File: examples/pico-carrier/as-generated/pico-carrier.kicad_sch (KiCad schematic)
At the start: 9 parts, among them J1 5V IN, J3 GP0-GP15, J4 GP16-GP28, PWR, U1 Pico

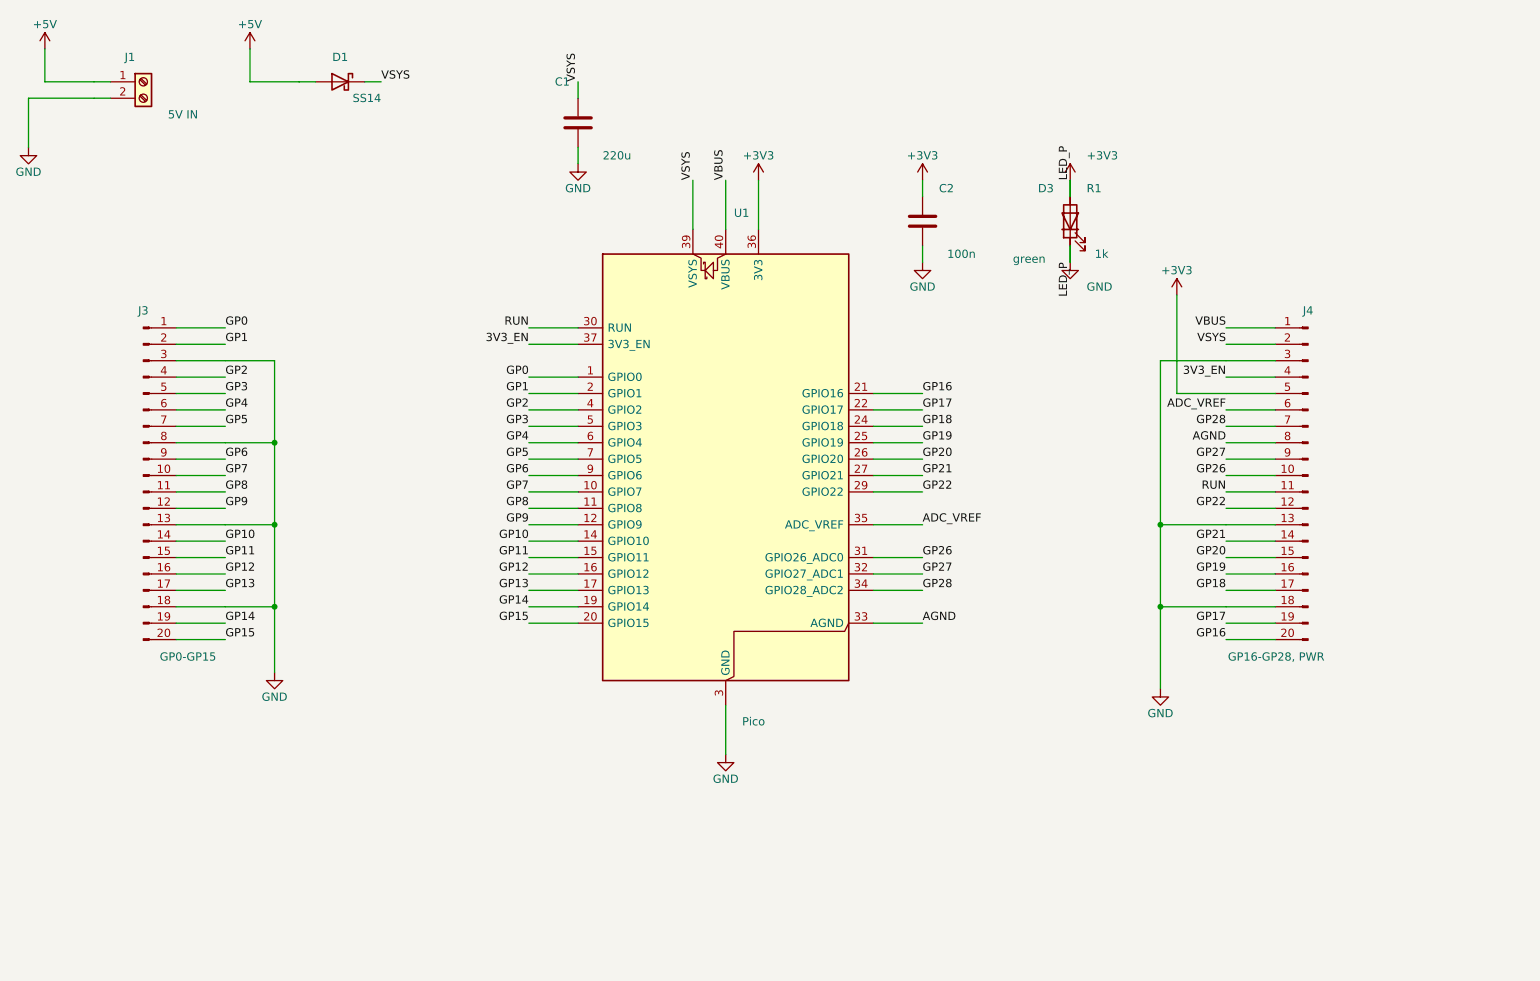
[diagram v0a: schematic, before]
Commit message: Relieve the pads, fillet the joints, and give the board its screw holes
Three of the reviewer's manufacturing points, and they largely fall out
of the one before it - once KiCad fills the plane, the thermal relief it
was already asked for in the file actually appears.

**Thermal relief.** The zones said thermal all along; our own filler
ignored it and flooded every land solid. KiCad's does not, so every
through-hole ground pad now sits in a gap bridged by four spokes and an
iron can bring the joint up without heating a hundred square millimetres
of copper. `layout.solid_pad_connection` reports the setting when a
board turns it off: drilled pads only, because a surface pad reflows in
an oven that is heating the plane anyway and flooding it is often the
better thermal answer.

**Teardrops.** A track entering a land is a step change in width, and a
step change is where copper tears - the connector gets levered on and
off, the drill wanders, and the crack starts at the corner. `_teardrops`
replaces the first stretch of each run with a three-step taper into the
land, checked against its neighbours before it is kept, so a fillet
never eats the clearance a fine-pitch escape needs. It *replaces* rather
than overlays: laying the taper on top of the run drew the same copper
twice, and `route.acute_angle` reported all thirty of them, correctly.
`route.mixed_track_widths` learns what a fillet looks like so a properly
filleted board does not read as one nobody decided the width of.

**Mounting holes.** Four M3 holes near the corners, placed before the
router runs because they are obstacles, and slid along the edges or a
little inboard where a connector body has the corner - the motor board
and the op-amp take three, which is what those floorplans have room for.
Grounded on the motor driver, whose chassis is metal and part of the
shield, plain on the rest: bonding the enclosure to the reference is the
enclosure's decision, not the board's.

Two things that fell out of placing par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
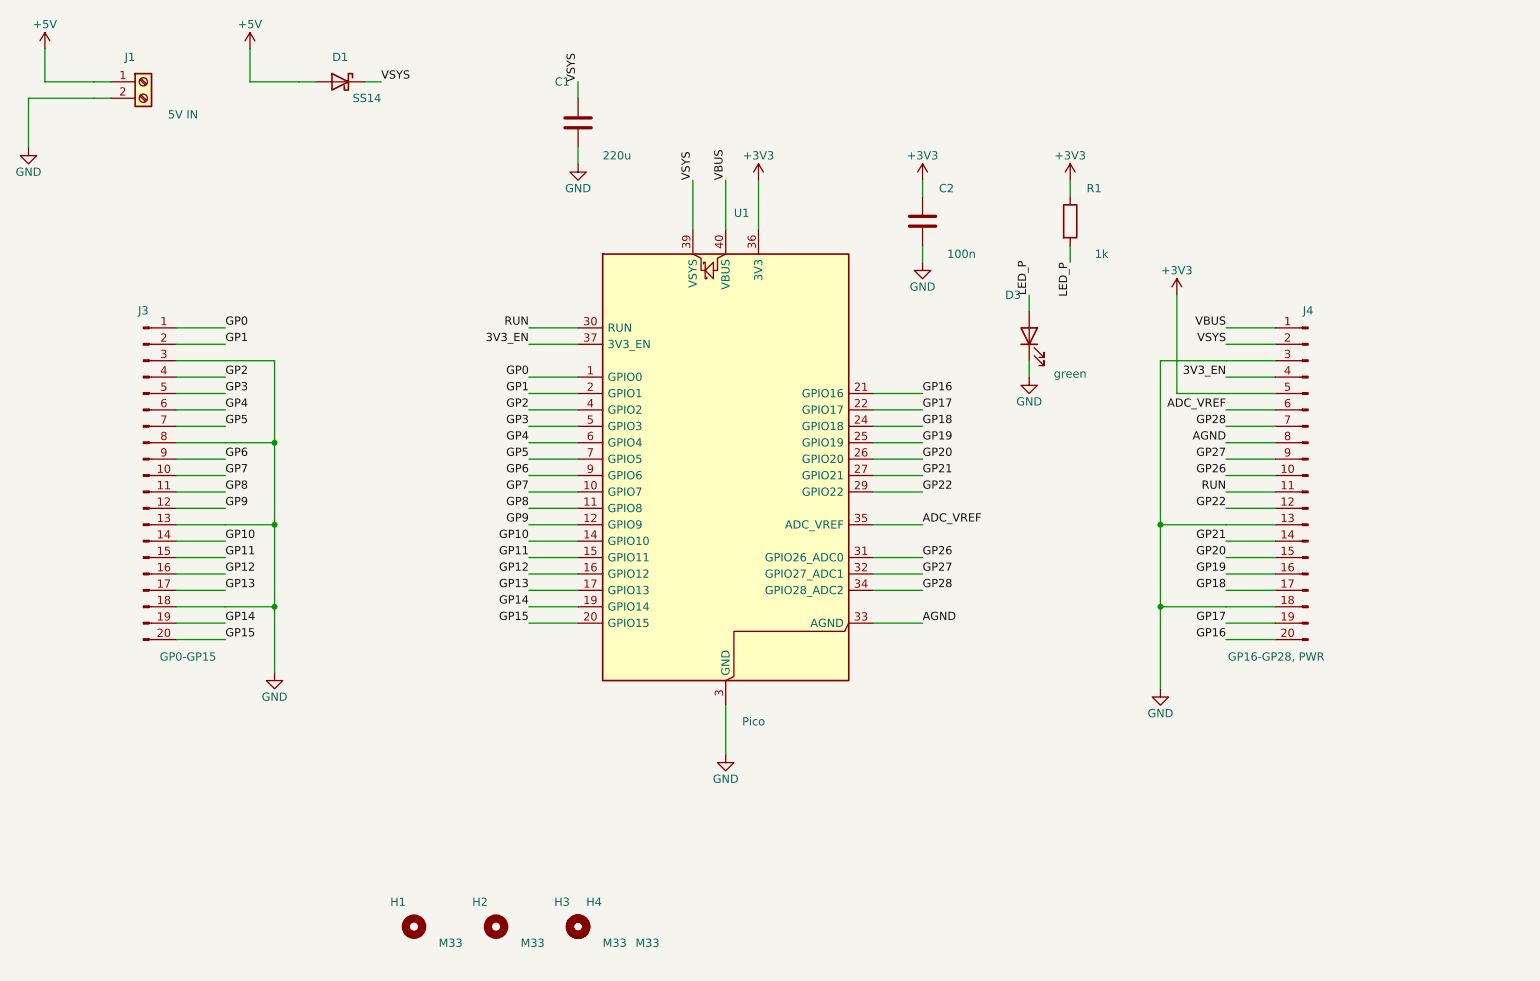
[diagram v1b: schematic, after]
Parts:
- added H1, H2, H3, H4: M33, MountingHole:MountingHole_3.2mm_M3, symbol Mechanical:MountingHole
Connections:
- net +3V3: no longer C1.2, C2.2, D3.1 (K), D3.2 (A), J1.2 (Pin_2), J3.13 (Pin_13), J3.18 (Pin_18), J3.3 (Pin_3), J3.8 (Pin_8), J4.13 (Pin_13), J4.18 (Pin_18), J4.3 (Pin_3), R1.2, U1.13 (GND), U1.18 (GND), U1.23 (GND), U1.28 (GND), U1.3 (GND), U1.38 (GND), U1.8 (GND)
- new net GND: C1.2, C2.2, D3.1 (K), J1.2 (Pin_2), J3.13 (Pin_13), J3.18 (Pin_18), J3.3 (Pin_3), J3.8 (Pin_8), J4.13 (Pin_13), J4.18 (Pin_18), J4.3 (Pin_3), U1.13 (GND), U1.18 (GND), U1.23 (GND), U1.28 (GND), U1.3 (GND), U1.38 (GND), U1.8 (GND)
- new net LED_P: D3.2 (A), R1.2
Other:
- moved on the sheet: D3
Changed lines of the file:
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@@
     (instances (project "pico-carrier" (path "/f86b03a2-2f64-5dc5-a6a7-b575bc25ae3a" (reference "R1") (unit 1))))
   )
-  (wire (pts (xy 203.51 64.58) (xy 203.51 67.12)) (stroke (width 0) (type default)))
-  (wire (pts (xy 203.51 56.96) (xy 203.51 54.42)) (stroke (width 0) (type default)))
-  (label "LED_P" (at 203.51 54.42 90) (effects (font (size 1.27 1.27)) (justify left bottom)))
-  (symbol (lib_id "Device:LED") (at 203.51 60.77 90.0) (unit 1)
+  (wire (pts (xy 197.16 82.36) (xy 197.16 84.9)) (stroke (width 0) (type default)))
+  (wire (pts (xy 197.16 74.74) (xy 197.16 72.2)) (stroke (width 0) (type default)))
+  (label "LED_P" (at 197.16 72.2 90) (effects (font (size 1.27 1.27)) (justify left bottom)))
+  (symbol (lib_id "Device:LED") (at 197.16 78.55 90.0) (unit 1)
     (exclude_from_sim no) (in_bom yes) (on_board yes) (dnp no)
-    (property "Reference" "D3" (at 200.97 55.69 90) (effects (font (size 1.27 1.27)) (justify left)))
-    (property "Value" "green" (at 199.7 66.612 90) (effects (font (size 1.27 1.27)) (justify left)))
-    (property "Footprint" "LED_SMD:LED_0805_2012Metric" (at 203.51 60.77 0) (effects (font (size 1.27 1.27)) hide))
-    (property "Datasheet" "https://optoelectronics.liteon.com/upload/download/DS-22-98-0002/LTST-C170KGKT.pdf" (at 203.51 60.77 0) (effects (font (size 1.27 1.27)) hide))
+    (property "Reference" "D3" (at 195.89 72.2 90) (effects (font (size 1.27 1.27)) (justify left)))
+    (property "Value" "green" (at 200.97 84.392 90) (effects (font (size 1.27 1.27)) (justify right)))
+    (property "Footprint" "LED_SMD:LED_0805_2012Metric" (at 197.16 78.55 0) (effects (font (size 1.27 1.27)) hide))
+    (property "Datasheet" "https://optoelectronics.liteon.com/upload/download/DS-22-98-0002/LTST-C170KGKT.pdf" (at 197.16 78.55 0) (effects (font (size 1.27 1.27)) hide))
     (pin "1" (uuid "634a87af-8e5f-58bb-80cb-050cf18f78ba-p1"))
     (pin "2" (uuid "634a87af-8e5f-58bb-80cb-050cf18f78ba-p2"))
     (instances (project "pico-carrier" (path "/f86b03a2-2f64-5dc5-a6a7-b575bc25ae3a" (reference "D3") (unit 1))))
+  )
+  (symbol (lib_id "Mechanical:MountingHole") (at 101.91 169.99 0.0) (unit 1)
+    (exclude_from_sim no) (in_bom yes) (on_board yes) (dnp no)
+    (property "Reference" "H1" (at 100.64 166.18 0) (effects (font (size 1.27 1.27)) (justify right)))
+    (property "Value" "M33" (at 105.72 172.53 0) (effects (font (size 1.27 1.27)) (justify left)))
+    (property "Footprint" "MountingHole:MountingHole_3.2mm_M3" (at 101.91 169.99 0) (effects (font (size 1.27 1.27)) hide))
+    (property "Datasheet" "~" (at 101.91 169.99 0) (effects (font (size 1.27 1.27)) hide))
+    (instances (project "pico-carrier" (path "/f86b03a2-2f64-5dc5-a6a7-b575bc25ae3a" (reference "H1") (unit 1))))
+  )
+  (symbol (lib_id "Mechanical:MountingHole") (at 114.61 169.99 0.0) (unit 1)
+    (exclude_from_sim no) (in_bom yes) (on_board yes) (dnp no)
+    (property "Reference" "H2" (at 113.34 166.18 0) (effects (font (size 1.27 1.27)) (justify right)))
+    (property "Value" "M33" (at 118.42 172.53 0) (effects (font (size 1.27 1.27)) (justify left)))
+    (property "Footprint" "MountingHole:MountingHole_3.2mm_M3" (at 114.61 169.99 0) (effects (font (size 1.27 1.27)) hide))
+    (property "Datasheet" "~" (at 114.61 169.99 0) (effects (font (size 1.27 1.27)) hide))
+    (instances (project "pico-carrier" (path "/f86b03a2-2f64-5dc5-a6a7-b575bc25ae3a" (reference "H2") (unit 1))))
+  )
+  (symbol (lib_id "Mechanical:MountingHole") (at 127.31 169.99 0.0) (unit 1)
+    (exclude_from_sim no) (in_bom yes) (on_board yes) (dnp no)
+    (property "Reference" "H3" (at 126.04 166.18 0) (effects (font (size 1.27 1.27)) (justify right)))
+    (property "Value" "M33" (at 131.12 172.53 0) (effects (font (size 1.27 1.27)) (justify left)))
+    (property "Footprint" "MountingHole:MountingHole_3.2mm_M3" (at 127.31 169.99 0) (effects (font (size 1.27 1.27)) hide))
+    (property "Datasheet" "~" (at 127.31 169.99 0) (effects (font (size 1.27 1.27)) hide))
+    (instances (project "pico-carrier" (path "/f86b03a2-2f64-5dc5-a6a7-b575bc25ae3a" (reference "H3") (unit 1))))
+  )
+  (symbol (lib_id "Mechanical:MountingHole") (at 127.31 169.99 0.0) (unit 1)
+    (exclude_from_sim no) (in_bom yes) (on_board yes) (dnp no)
+    (property "Reference" "H4" (at 128.58 166.18 0) (effects (font (size 1.27 1.27)) (justify left)))
+    (property "Value" "M33" (at 136.2 172.53 0) (effects (font (size 1.27 1.27)) (justify left)))
+    (property "Footprint" "MountingHole:MountingHole_3.2mm_M3" (at 127.31 169.99 0) (effects (font (size 1.27 1.27)) hide))
+    (property "Datasheet" "~" (at 127.31 169.99 0) (effects (font (size 1.27 1.27)) hide))
+    (instances (project "pico-carrier" (path "/f86b03a2-2f64-5dc5-a6a7-b575bc25ae3a" (reference "H4") (unit 1))))
   )
   (wire (pts (xy 72.7 82.36) (xy 80.32 82.36)) (stroke (width 0) (type default)))
@@
     (exclude_from_sim no) (in_bom no) (on_board yes) (dnp no)
     (property "Reference" "#PWR12" (at 203.51 54.42 0) (effects (font (size 1.27 1.27)) hide))
-    (property "Value" "+3V3" (at 206.05 50.61 0) (effects (font (size 1.27 1.27)) (justify left)))
+    (property "Value" "+3V3" (at 203.51 50.61 0) (effects (font (size 1.27 1.27))))
     (property "Footprint" "" (at 203.51 54.42 0) (effects (font (size 1.27 1.27)) hide))
     (property "Datasheet" "" (at 203.51 54.42 0) (effects (font (size 1.27 1.27)) hide))
@@
     (instances (project "pico-carrier" (path "/f86b03a2-2f64-5dc5-a6a7-b575bc25ae3a" (reference "#PWR12") (unit 1))))
   )
-  (symbol (lib_id "power:GND") (at 203.51 67.12 0) (unit 1)
+  (symbol (lib_id "power:GND") (at 197.16 84.9 0) (unit 1)
     (exclude_from_sim no) (in_bom no) (on_board yes) (dnp no)
-    (property "Reference" "#PWR13" (at 203.51 67.12 0) (effects (font (size 1.27 1.27)) hide))
-    (property "Value" "GND" (at 206.05 70.93 0) (effects (font (size 1.27 1.27)) (justify left)))
-    (property "Footprint" "" (at 203.51 67.12 0) (effects (font (size 1.27 1.27)) hide))
-    (property "Datasheet" "" (at 203.51 67.12 0) (effects (font (size 1.27 1.27)) hide))
+    (property "Reference" "#PWR13" (at 197.16 84.9 0) (effects (font (size 1.27 1.27)) hide))
+    (property "Value" "GND" (at 197.16 88.71 0) (effects (font (size 1.27 1.27))))
+    (property "Footprint" "" (at 197.16 84.9 0) (effects (font (size 1.27 1.27)) hide))
+    (property "Datasheet" "" (at 197.16 84.9 0) (effects (font (size 1.27 1.27)) hide))
     (pin "1" (uuid "bd382a54-694d-5007-a758-46e341ab7157-p"))
     (instances (project "pico-carrier" (path "/f86b03a2-2f64-5dc5-a6a7-b575bc25ae3a" (reference "#PWR13") (unit 1))))
